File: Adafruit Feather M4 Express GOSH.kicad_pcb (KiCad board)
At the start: 2 copper layers, 50.8 x 22.9 mm, 83 parts, among them Q3 DMG341, SW1 KMR2, U1 2MB Flash, U2 AP2112-3.3, U3 MCP73831T-2ACI/OT, X1 JSTPH, X2 32.768, X3 microUSB

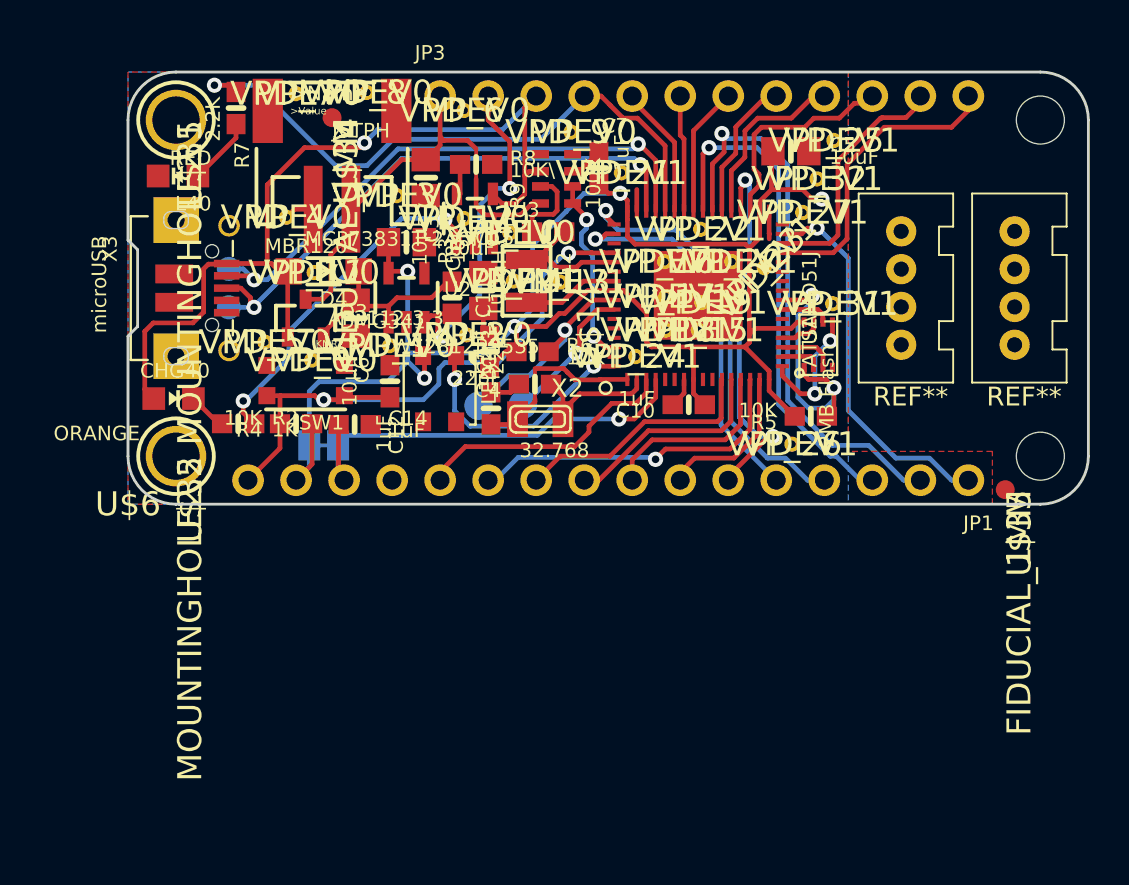
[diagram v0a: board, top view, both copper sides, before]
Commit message: finished routing
Got the grove connections routed, and passing DRC
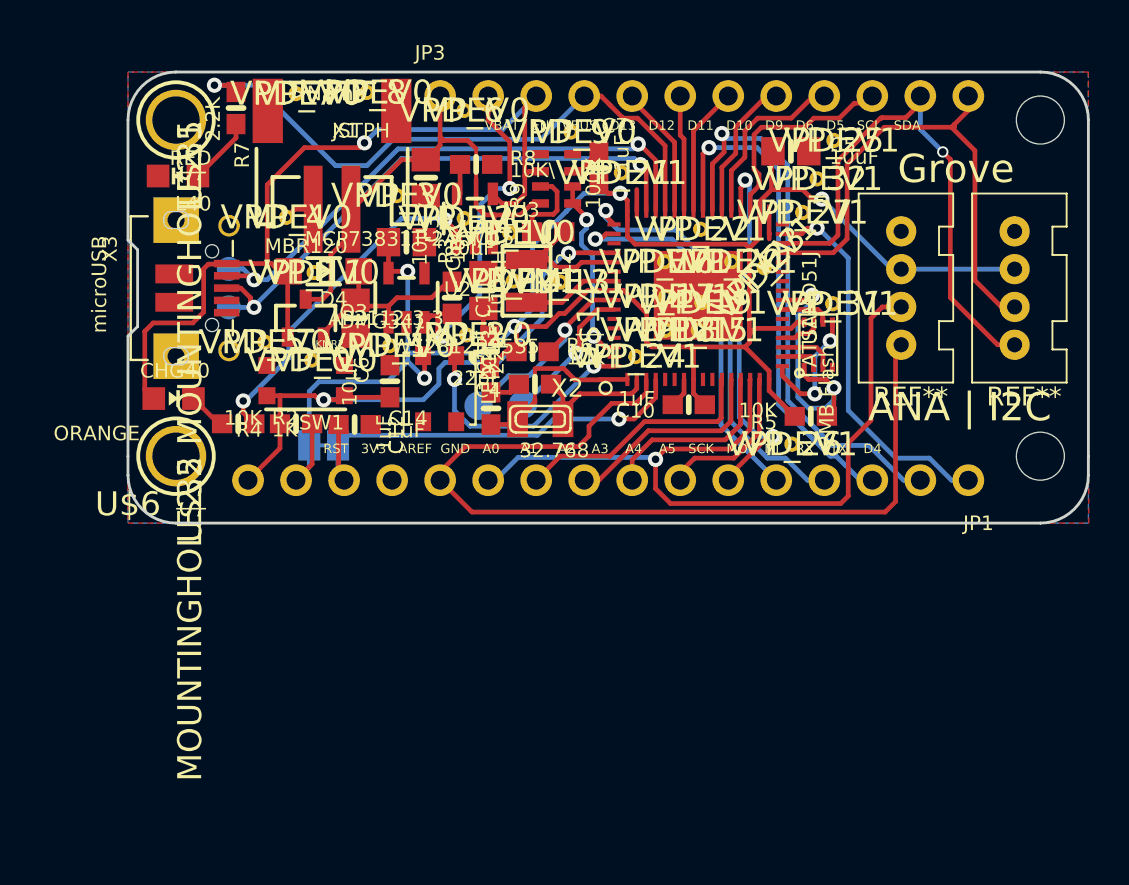
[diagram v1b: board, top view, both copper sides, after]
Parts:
- removed U$34, U$35: FIDUCIAL_1MM, FIDUCIAL_1MM
- moved U$13 2.53 mm to (126.9, 98.9)
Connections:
- X1 pad NC1: (no net) -> GND
- X1 pad NC2: (no net) -> GND
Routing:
- net A0: track 14.0 -> 47.5 mm
- net A1: track 17.7 -> 41.7 mm
- net SCL: track 13.1 -> 28.8 mm, vias 0 -> 1
- net +3V3: track 95.2 -> 106.9 mm
- net SDA: track 16.0 -> 27.6 mm
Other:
- board size 50.8 x 22.9 mm -> 50.8 x 23.9 mm
- board text added: "ANA | I2C"
- board text added: "GND 3V3 A1 A0"
- board text added: "GND 3V3 SDA SCL"
- board text added: "GOSH 2018 SHENZHEN"
- board text added: "Grove"
- board text added: "RST 3V3 AREF GND A0 A1 A2 A3 A4 A5 SCK MO MI RX TX D4"
- board text added: "Target: Feather M4 Express"
- board text added: "VBAT EN VBUS D13 D12 D11 D10 D9 D6 D5 SCL SDA"

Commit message: Added production process files from PCB pool
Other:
- board text added: "Needs modification to make bootloading easier? Or, needs small bootloader board w pins...?"
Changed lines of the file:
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@@
     (area 119.013448 91.74922 176.350815 135.06674)
     (thickness 1.6)
-    (drawings 148)
+    (drawings 149)
     (tracks 626)
     (zones 0)
@@
     (38 B.Mask user)
     (39 F.Mask user)
-    (40 Dwgs.User user hide)
-    (41 Cmts.User user hide)
+    (40 Dwgs.User user)
+    (41 Cmts.User user)
     (42 Eco1.User user)
     (43 Eco2.User user)
@@
     (aux_axis_origin 0 0)
     (grid_origin 184.2 95.6)
-    (visible_elements FFFCFF7F)
+    (visible_elements FFFCBF7F)
     (pcbplotparams
       (layerselection 0x010fc_80000001)
@@
       (net 1 GND))
   )
+  (gr_text "Needs modification to make bootloading easier?\nOr, needs small bootloader board w pins...?" (at 150 122.1) (layer Dwgs.User)
+    (effects (font (size 1.5 1.5) (thickness 0.3)))
+  )
   (gr_text "Target: Feather M4 Express" (at 146 98.6) (layer B.SilkS)
